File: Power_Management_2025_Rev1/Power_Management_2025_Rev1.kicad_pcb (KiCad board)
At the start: 2 copper layers, 213 x 164.6 mm, 100 parts, among them J1 RJ45_LED_Shielded, Q1 BSS138, Q2 IPB180N10S4-02, Q3 IPB180N10S4-02, Q4 IPB180N10S4-02, U1 Teensy4.1_DEV-16771, U10 LT1910, U11 LT1910, U12 PKE3316ZPI, U13 PKE3316ZPI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

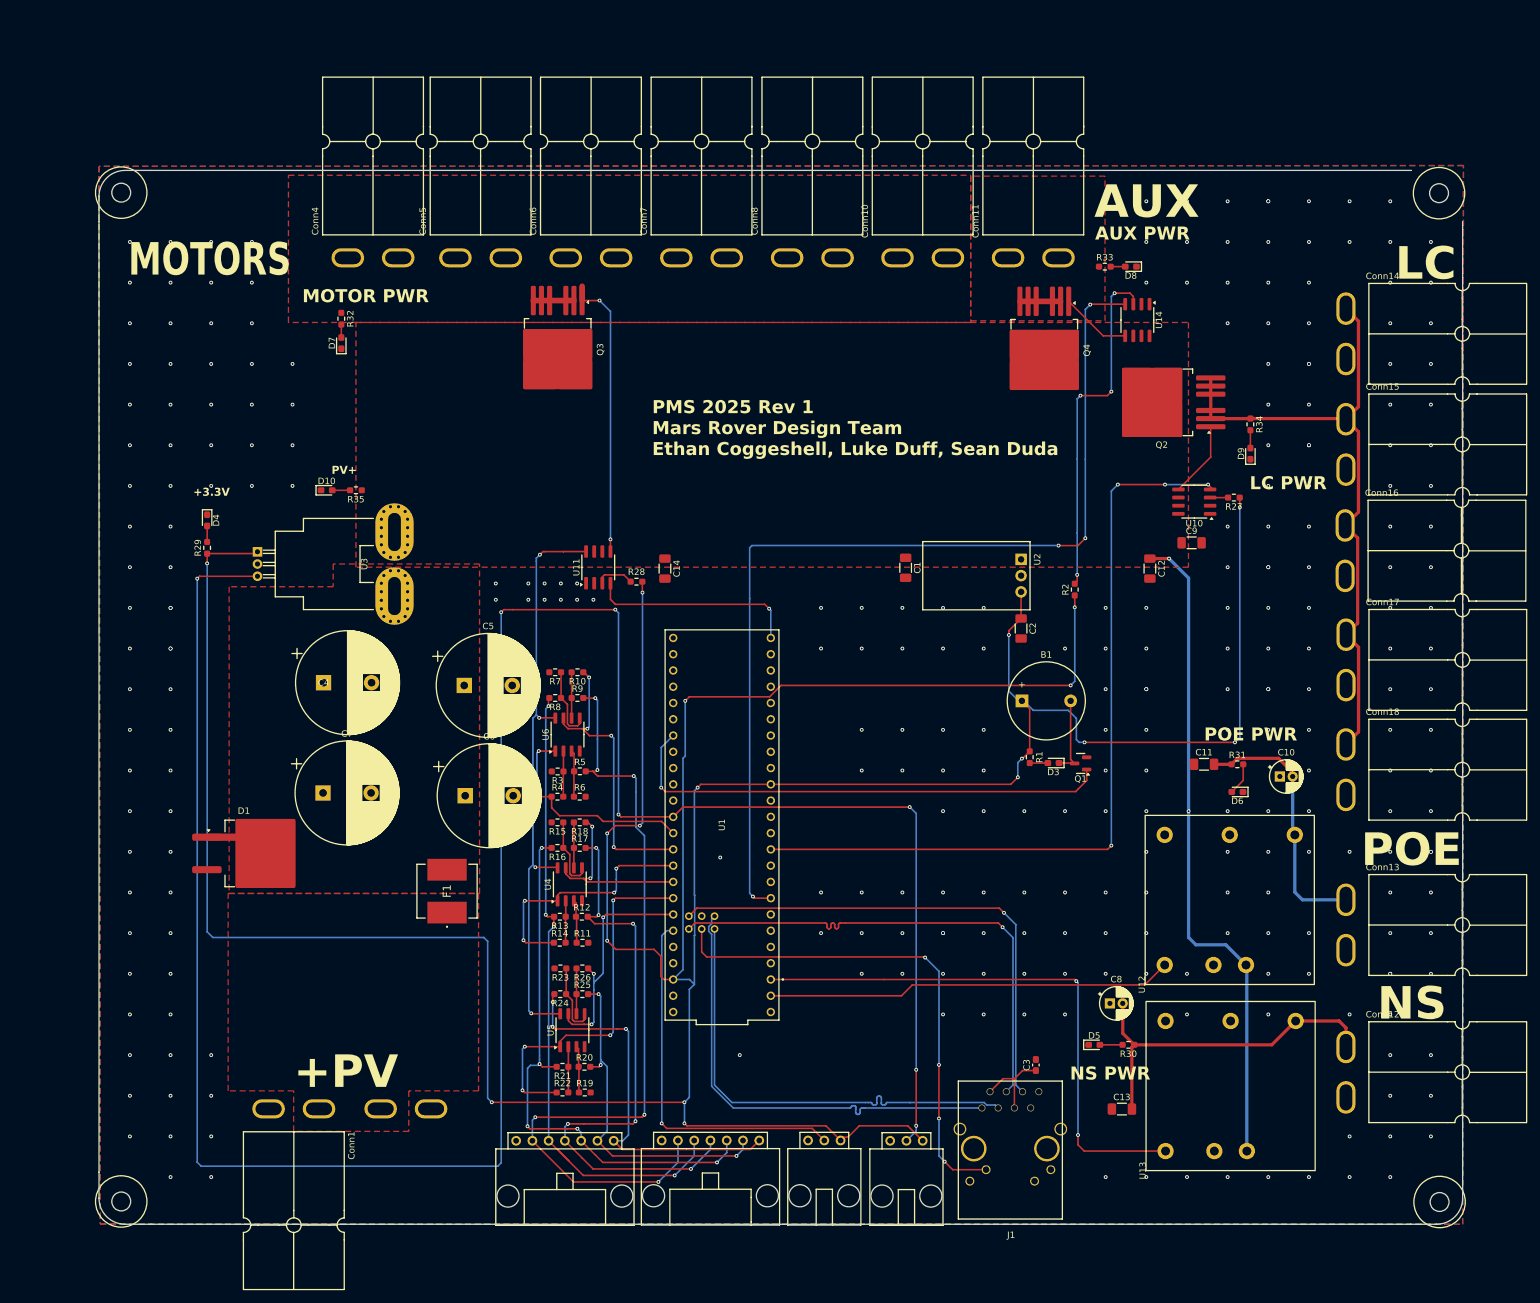
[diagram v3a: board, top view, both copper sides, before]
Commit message: Rerouted problematic traces,  made low current power plane, added vias in open areas, added signature
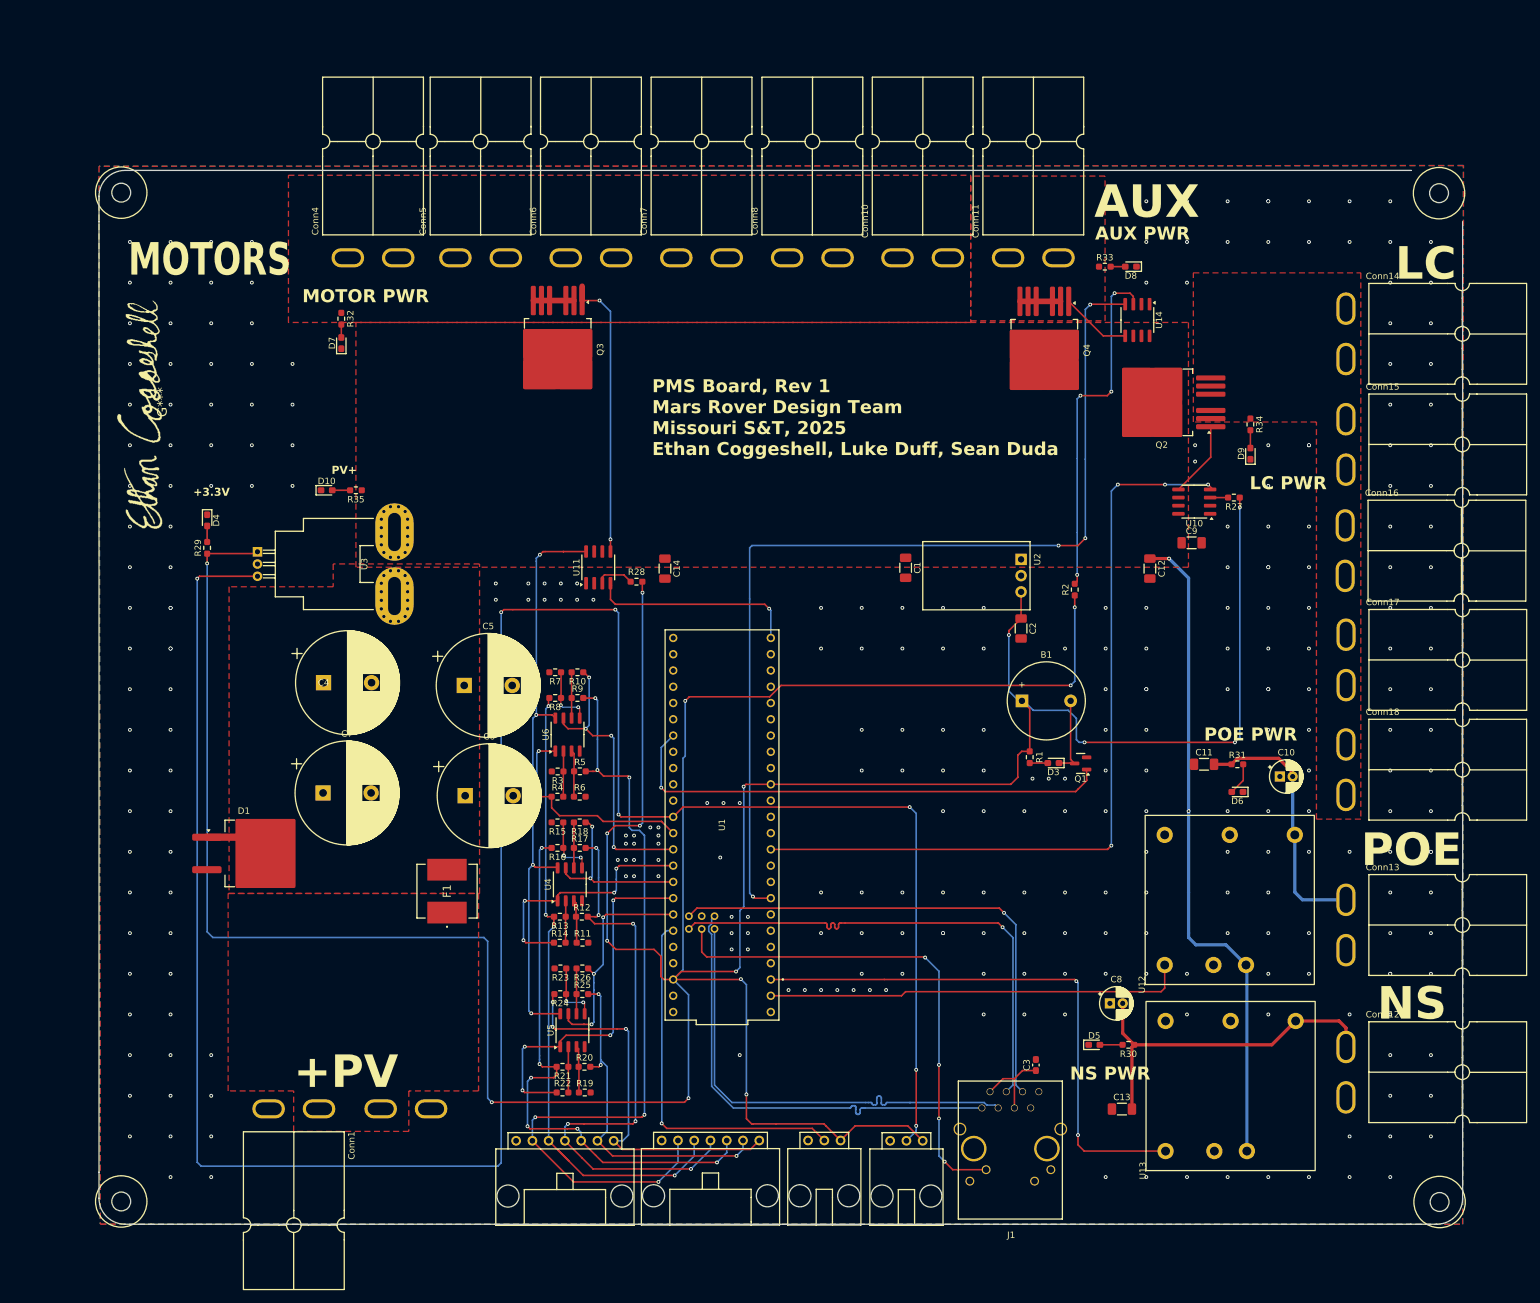
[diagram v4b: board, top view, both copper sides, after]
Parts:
- added G***: LOGO, LOGO, F.Cu at (36.8, 63.1)
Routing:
- net LOW_CURRENT_PWR: track 102.4 -> 0.00 mm
- net +3.3V: track 618.5 -> 638.4 mm
- net POE_ENABLE: track 63.5 -> 65.6 mm
- net CELL4: track 86.4 -> 88.5 mm, vias 5 -> 6
- net Net-(U5B-+): track 11.7 -> 9.73 mm, vias 0 -> 2
- net Net-(U4B-+): track 11.5 -> 9.68 mm, vias 0 -> 2
- net Net-(U6B-+): track 11.5 -> 9.80 mm, vias 0 -> 2
- net CELL_SENSE_6: track 36.1 -> 34.8 mm
- net CELL_SENSE_4: track 29.5 -> 28.4 mm
- net CELL_SENSE_2: track 46.3 -> 45.6 mm
- net GND: vias 280 -> 303
- added copper zone on F.Cu, net LOW_CURRENT_PWR
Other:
- board text added: "PMS Board, Rev 1 Mars Rover Design Team Missouri S&T, 2025 Ethan Coggeshell, Luke Duff, Sean Duda"
- board text removed: "PMS 2025 Rev 1 Mars Rover Design Team Ethan Coggeshell, Luke Duff, Sean Duda"

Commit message: Few board rev changes
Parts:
- U2: footprint Converter_DCDC:Converter_DCDC_Murata_OKI-78SR_Horizontal -> MRDT_Devices:OKI_Horizontal
- moved D7 2.20 mm to (64.7, 56.1)
- moved R32 0.69 mm to (64.7, 50.8)
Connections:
- U1 pad TX+: TX+ -> (no net)
- U1 pad TX-: TX- -> (no net)
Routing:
- net +3.3V: track 638.4 -> 684.5 mm
- net AUX_PWR: track 6.35 -> 0.00 mm
- net MOTOR_PWR: track 6.35 -> 0.00 mm
- net TX-: track 72.8 -> 71.0 mm
- net TX+: track 72.9 -> 71.4 mm
- net Net-(D7-A): track 2.02 -> 3.53 mm
- net LED: track 79.0 -> 79.8 mm, vias 4 -> 2
- net GND: vias 303 -> 280

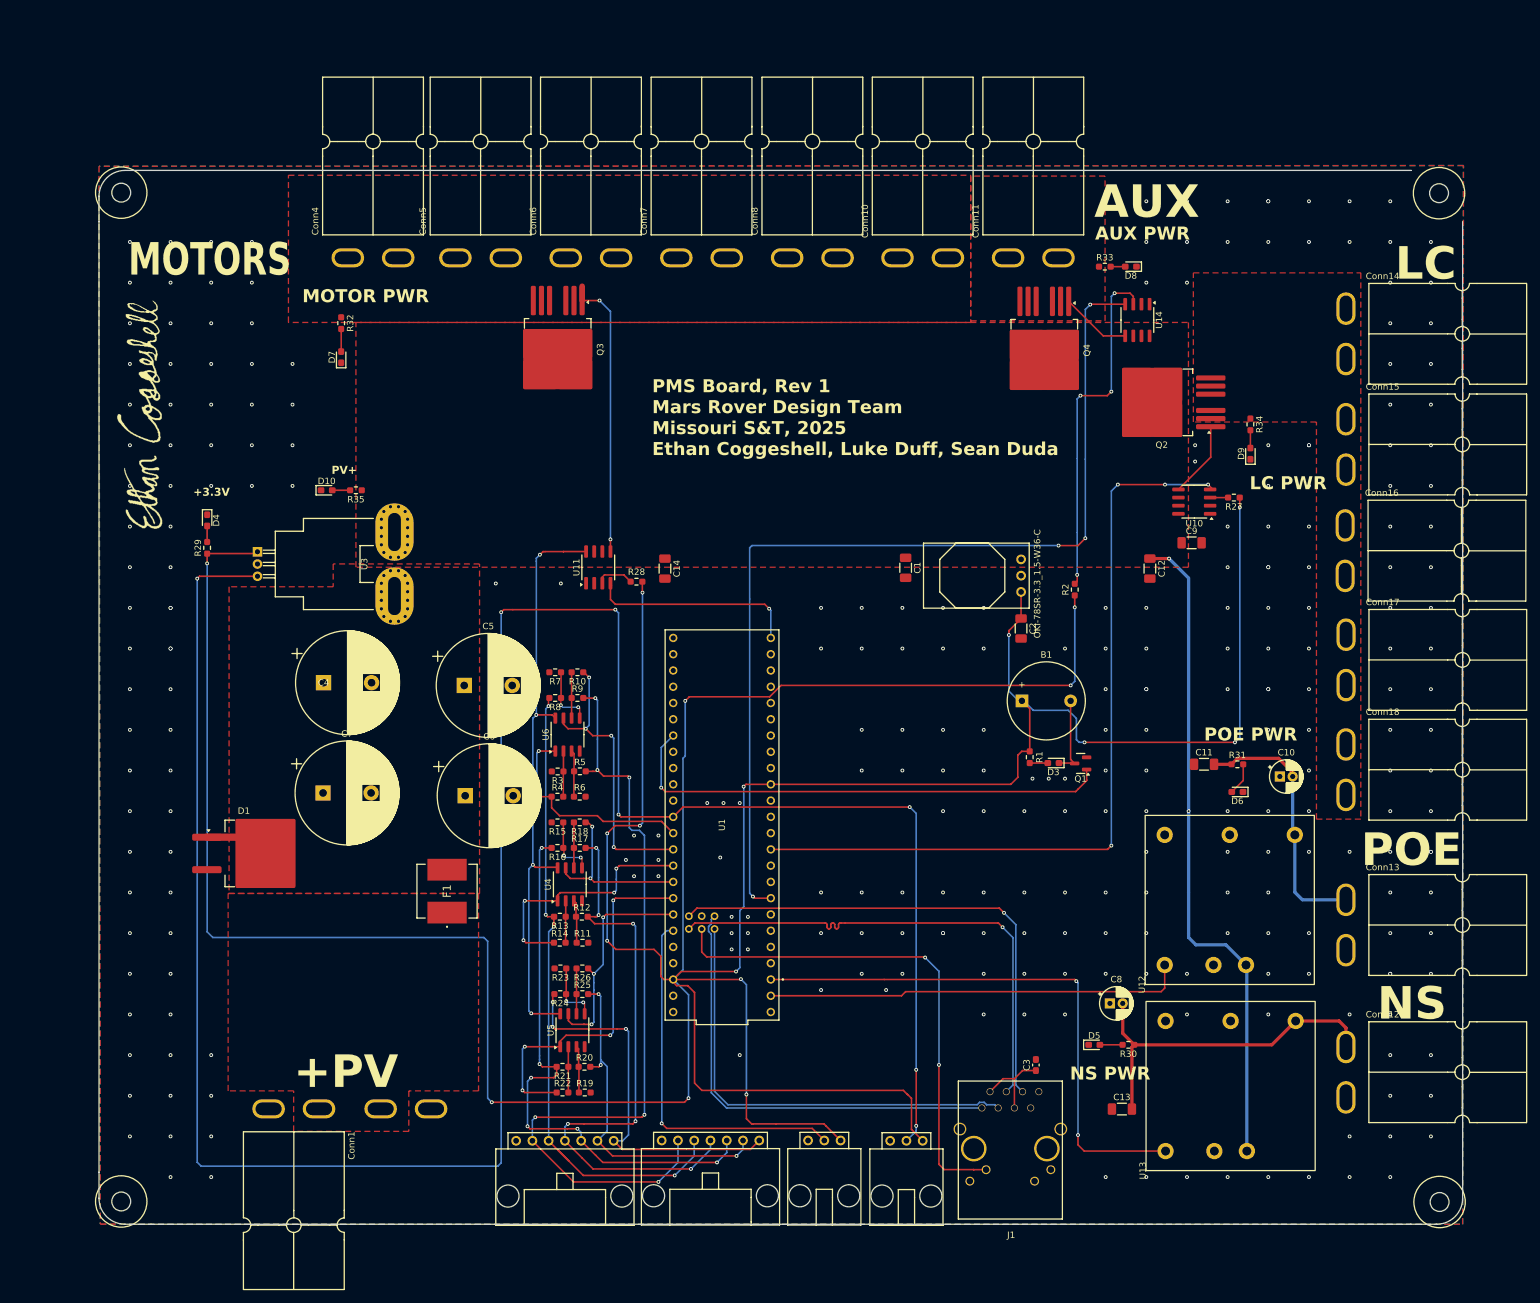
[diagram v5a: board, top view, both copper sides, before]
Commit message: Made some changes that were mentioned at board review. +3.3V still needs to be traced
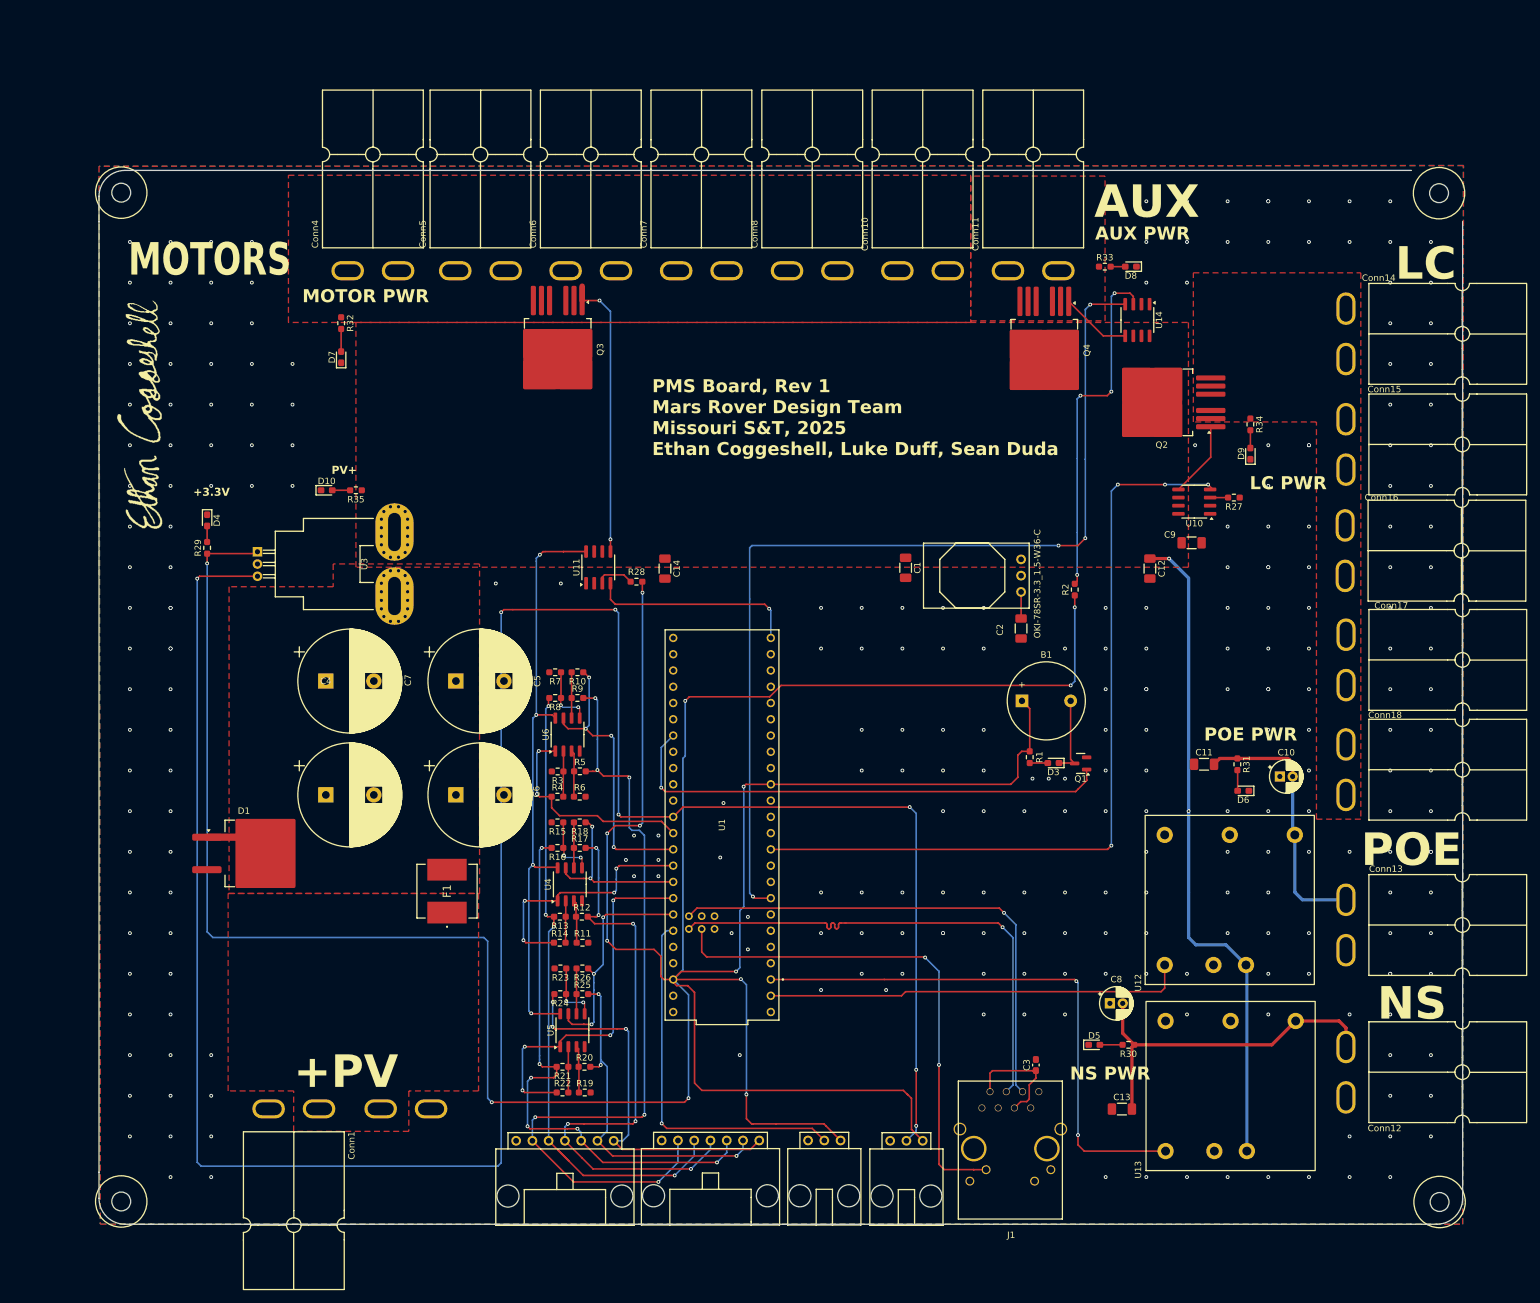
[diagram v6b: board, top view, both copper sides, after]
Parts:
- moved Conn10 2.02 mm to (159.8, 42.7)
- moved Conn11 2.02 mm to (177.1, 42.7)
- moved Conn5 2.02 mm to (90.7, 42.7)
- moved Conn6 2.02 mm to (108.0, 42.7)
- moved Conn7 2.02 mm to (125.2, 42.7)
- moved Conn8 2.02 mm to (142.6, 42.7)
- moved Conn4 2.02 mm to (73.9, 42.7)
- moved C5 1.47 mm to (82.7, 106.7)
- moved C6 1.45 mm to (82.7, 124.5)
- moved D6 0.93 mm to (205.6, 123.8)
- moved C7 0.53 mm to (62.4, 124.5)
- moved C4 0.44 mm to (62.4, 106.7)
- turned R31 to -90 degrees
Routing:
- net +3.3V: track 684.5 -> 593.3 mm, vias 18 -> 14
- net TX+: track 71.4 -> 0.00 mm
- net TX-: track 71.0 -> 0.00 mm
- net Net-(C3-Pad1): track 13.1 -> 18.0 mm
- net Net-(D6-A): track 5.06 -> 3.25 mm
- net POE_24V: track 40.9 -> 41.7 mm
- net GND: vias 280 -> 274

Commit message: Board review changes
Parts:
- moved C5 15.1 mm to (67.6, 106.9)
- moved C4 11.7 mm to (50.6, 107.0)
- moved C6 7.01 mm to (76.4, 121.4)
- moved C7 4.45 mm to (59.1, 121.4)
- moved Q3 3.18 mm to (98.5, 58.1)
- moved Q4 3.05 mm to (174.6, 58.1)
- moved Conn11 2.55 mm to (177.1, 45.3)
- moved Conn6 2.55 mm to (108.1, 45.3)
- moved Conn7 2.55 mm to (125.3, 45.3)
- moved Conn8 2.55 mm to (142.6, 45.3)
- moved Conn10 2.55 mm to (159.9, 45.3)
- moved Conn4 2.55 mm to (74.0, 45.3)
- moved Conn5 2.55 mm to (90.8, 45.3)
- moved U14 1.75 mm to (189.1, 52.0)
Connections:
- U1 pad TX+: (no net) -> TX+
- U1 pad TX-: (no net) -> TX-
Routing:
- net +3.3V: track 593.3 -> 699.9 mm
- net TX+: track 0.00 -> 75.0 mm
- net TX-: track 0.00 -> 74.2 mm
- net Net-(U14-FAULT): track 54.8 -> 49.3 mm, vias 4 -> 2
- net Net-(Q3-G): track 44.9 -> 40.1 mm
- net AUX_EN: track 152.9 -> 150.0 mm
- net Net-(Q4-G): track 11.1 -> 12.3 mm
- net CURRENT_SENSE: track 384.3 -> 383.1 mm
